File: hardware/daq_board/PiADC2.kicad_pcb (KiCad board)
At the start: 2 copper layers, 65 x 56 mm, 67 parts, among them J1 Pi GPIO, J2 ADCIN1, J3 ADCIN2, J4 ISO_IN, J6 I2C_OUT, SW1 SW_Push, SW2 SW_Push, U1 ADS1115IDGS, U2 TCA9517, U3 ADS1115IDGS, U4 24LC16, U5 MCP79401-I_SN, U6 MCP23008T-E_SS, U7 HCPL2631M, U8 HCPL2631M, Y1 Crystal

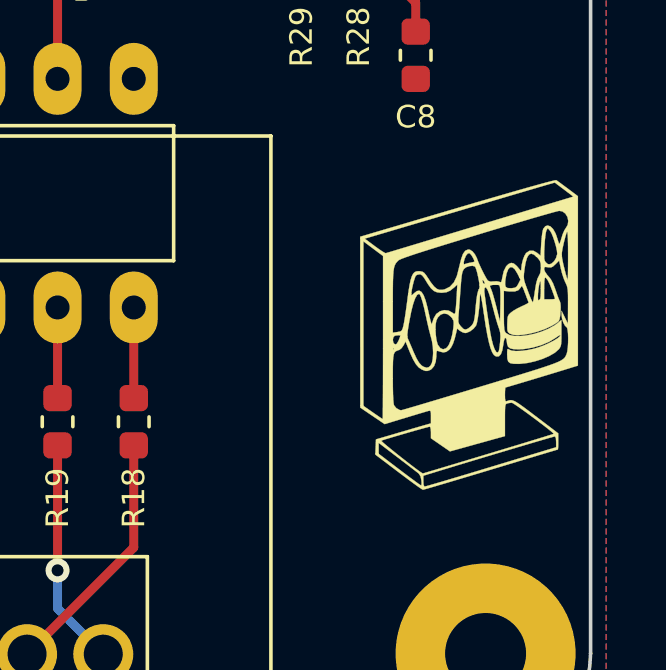
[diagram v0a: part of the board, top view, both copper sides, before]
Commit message: completed breakout board and updated daq board to version 2
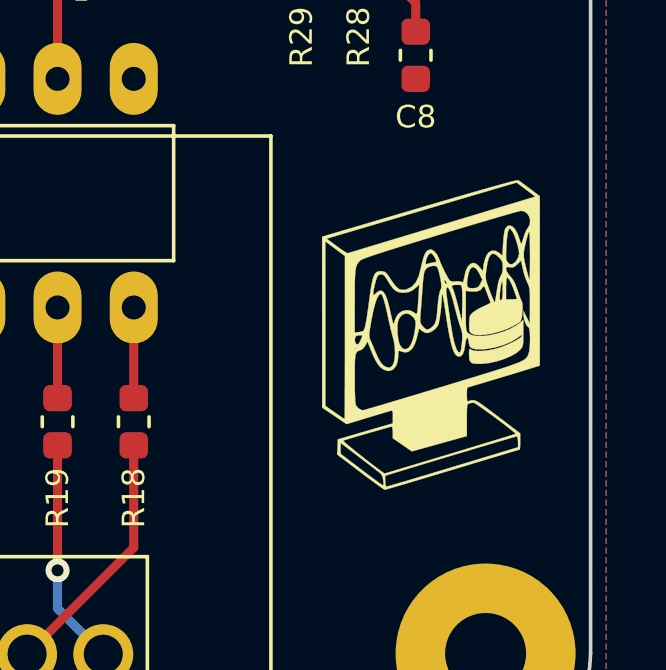
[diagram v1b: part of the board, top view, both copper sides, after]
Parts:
- moved LOGO1 1.27 mm to (166.9, 115.8)
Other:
- board text added: "FOR TESTING OR LABORATORY USE ONLY OPEN SOURCE HARDWARE RELEASED UNDER CERN OHL v1.2"
- board text added: "PiADC2 v2 CapConiX LLC capconix.com"
- board text removed: "FOR TESTING ONLY OPEN SOURCE HARDWARE RELEASED UNDER CERN OHL v1.2"
- board text removed: "PiADC2 v1 CapConiX LLC capconix.com"
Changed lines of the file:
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@@
   )
   (setup
-    (last_trace_width 0.3)
+    (last_trace_width 0.25)
     (user_trace_width 0.3)
     (trace_clearance 0.2)
@@
       (effects (font (size 0.75 0.75) (thickness 0.15)))
     )
-    (fp_text value ISO_IN (at 0 -4.445) (layer F.Fab)
+    (fp_text value ISO_IN (at 0 -4.445) (layer F.Fab) hide
       (effects (font (size 1 1) (thickness 0.15)))
     )
@@
   )
   (module CapConiX_Logos:CapConiX_Logo_10_7 (layer F.Cu)
-    (at 168.148 115.824)
+    (at 166.878 115.824)
     (fp_text reference LOGO1 (at 0 0) (layer F.SilkS) hide
       (effects (font (size 0.75 0.75) (thickness 0.3)))
@@
     )
   )
-  (gr_text "PiADC2 v1\nCapConiX LLC\ncapconix.com" (at 167.894 116.332 270) (layer B.SilkS)
+  (gr_text "PiADC2 v2\nCapConiX LLC\ncapconix.com" (at 166.878 116.332 270) (layer B.SilkS)
     (effects (font (size 1 1) (thickness 0.25)) (justify mirror))
   )
-  (gr_text "FOR TESTING ONLY\nOPEN SOURCE HARDWARE\nRELEASED UNDER CERN OHL v1.2" (at 148.59 101.6) (layer B.SilkS)
+  (gr_text "FOR TESTING OR LABORATORY USE ONLY\nOPEN SOURCE HARDWARE\nRELEASED UNDER CERN OHL v1.2" (at 148.59 101.6) (layer B.SilkS)
     (effects (font (size 1 1) (thickness 0.25)) (justify mirror))
   )
@@
   (segment (start 121.92 97.282) (end 121.928 97.29) (width 0.3) (layer F.Cu) (net 31))
   (segment (start 121.92 96.266) (end 121.92 97.282) (width 0.3) (layer F.Cu) (net 31))
+  (segment (start 119.6595 98.806) (end 120.65 98.806) (width 0.3) (layer F.Cu) (net 32))
+  (segment (start 120.65 98.806) (end 120.904 99.06) (width 0.3) (layer F.Cu) (net 32))
+  (segment (start 125.492 98.998) (end 125.492 98.298) (width 0.3) (layer F.Cu) (net 32))
+  (segment (start 125.43 99.06) (end 125.492 98.998) (width 0.3) (layer F.Cu) (net 32))
+  (segment (start 120.904 99.06) (end 125.43 99.06) (width 0.3) (layer F.Cu) (net 32))
+  (segment (start 121.003 97.926) (end 121.428 97.926) (width 0.3) (layer F.Cu) (net 32))
+  (segment (start 120.65 98.279) (end 121.003 97.926) (width 0.3) (layer F.Cu) (net 32))
+  (segment (start 120.65 98.806) (end 120.65 98.279) (width 0.3) (layer F.Cu) (net 32))
   (segment (start 119.6595 101.346) (end 120.65 101.346) (width 0.3) (layer F.Cu) (net 33))
   (segment (start 120.65 101.346) (end 120.904 101.092) (width 0.3) (layer F.Cu) (net 33))
@@
   (segment (start 120.65 101.873) (end 121.003 102.226) (width 0.3) (layer F.Cu) (net 33))
   (segment (start 120.65 101.346) (end 120.65 101.873) (width 0.3) (layer F.Cu) (net 33))
+  (segment (start 119.6595 103.886) (end 121.92 103.886) (width 0.3) (layer F.Cu) (net 34))
+  (segment (start 123.444 105.41) (end 125.492 105.41) (width 0.3) (layer F.Cu) (net 34))
+  (segment (start 121.92 103.886) (end 123.444 105.41) (width 0.3) (layer F.Cu) (net 34))
+  (segment (start 121.928 103.878) (end 121.92 103.886) (width 0.3) (layer F.Cu) (net 34))
+  (segment (start 121.928 102.226) (end 121.928 103.878) (width 0.3) (layer F.Cu) (net 34))
   (segment (start 121.92 115.824) (end 121.928 115.832) (width 0.3) (layer F.Cu) (net 35))
   (segment (start 121.928 115.832) (end 121.928 116.468) (width 0.3) (layer F.Cu) (net 35))
@@
   (segment (start 121.92 114.808) (end 123.444 113.284) (width 0.3) (layer F.Cu) (net 35))
   (segment (start 121.92 114.808) (end 121.92 115.824) (width 0.3) (layer F.Cu) (net 35))
-  (segment (start 125.43 119.634) (end 125.492 119.696) (width 0.3) (layer F.Cu) (net 37))
-  (segment (start 125.492 119.696) (end 125.492 120.396) (width 0.3) (layer F.Cu) (net 37))
-  (segment (start 121.003 120.768) (end 121.428 120.768) (width 0.3) (layer F.Cu) (net 37))
-  (segment (start 120.904 119.634) (end 125.43 119.634) (width 0.3) (layer F.Cu) (net 37))
-  (segment (start 120.65 119.888) (end 120.65 120.415) (width 0.3) (layer F.Cu) (net 37))
-  (segment (start 120.65 120.415) (end 121.003 120.768) (width 0.3) (layer F.Cu) (net 37))
-  (segment (start 119.6595 119.888) (end 120.65 119.888) (width 0.3) (layer F.Cu) (net 37))
-  (segment (start 120.65 119.888) (end 120.904 119.634) (width 0.3) (layer F.Cu) (net 37))
-  (segment (start 119.6595 98.806) (end 120.65 98.806) (width 0.3) (layer F.Cu) (net 32))
-  (segment (start 120.65 98.806) (end 120.904 99.06) (width 0.3) (layer F.Cu) (net 32))
-  (segment (start 125.492 98.998) (end 125.492 98.298) (width 0.3) (layer F.Cu) (net 32))
-  (segment (start 125.43 99.06) (end 125.492 98.998) (width 0.3) (layer F.Cu) (net 32))
-  (segment (start 120.904 99.06) (end 125.43 99.06) (width 0.3) (layer F.Cu) (net 32))
-  (segment (start 121.003 97.926) (end 121.428 97.926) (width 0.3) (layer F.Cu) (net 32))
-  (segment (start 120.65 98.279) (end 121.003 97.926) (width 0.3) (layer F.Cu) (net 32))
-  (segment (start 120.65 98.806) (end 120.65 98.279) (width 0.3) (layer F.Cu) (net 32))
-  (segment (start 119.6595 103.886) (end 121.92 103.886) (width 0.3) (layer F.Cu) (net 34))
-  (segment (start 123.444 105.41) (end 125.492 105.41) (width 0.3) (layer F.Cu) (net 34))
-  (segment (start 121.92 103.886) (end 123.444 105.41) (width 0.3) (layer F.Cu) (net 34))
-  (segment (start 121.928 103.878) (end 121.92 103.886) (width 0.3) (layer F.Cu) (net 34))
-  (segment (start 121.928 102.226) (end 121.928 103.878) (width 0.3) (layer F.Cu) (net 34))
   (segment (start 119.6595 117.348) (end 120.65 117.348) (width 0.3) (layer F.Cu) (net 36))
   (segment (start 120.65 116.821) (end 121.003 116.468) (width 0.3) (layer F.Cu) (net 36))
@@
   (segment (start 120.65 117.348) (end 120.65 116.821) (width 0.3) (layer F.Cu) (net 36))
   (segment (start 125.492 117.54) (end 125.492 116.84) (width 0.3) (layer F.Cu) (net 36))
+  (segment (start 125.43 119.634) (end 125.492 119.696) (width 0.3) (layer F.Cu) (net 37))
+  (segment (start 125.492 119.696) (end 125.492 120.396) (width 0.3) (layer F.Cu) (net 37))
+  (segment (start 121.003 120.768) (end 121.428 120.768) (width 0.3) (layer F.Cu) (net 37))
+  (segment (start 120.904 119.634) (end 125.43 119.634) (width 0.3) (layer F.Cu) (net 37))
+  (segment (start 120.65 119.888) (end 120.65 120.415) (width 0.3) (layer F.Cu) (net 37))
+  (segment (start 120.65 120.415) (end 121.003 120.768) (width 0.3) (layer F.Cu) (net 37))
+  (segment (start 119.6595 119.888) (end 120.65 119.888) (width 0.3) (layer F.Cu) (net 37))
+  (segment (start 120.65 119.888) (end 120.904 119.634) (width 0.3) (layer F.Cu) (net 37))
   (segment (start 123.444 123.952) (end 125.492 123.952) (width 0.3) (layer F.Cu) (net 38))
   (segment (start 119.6595 122.428) (end 121.92 122.428) (width 0.3) (layer F.Cu) (net 38))

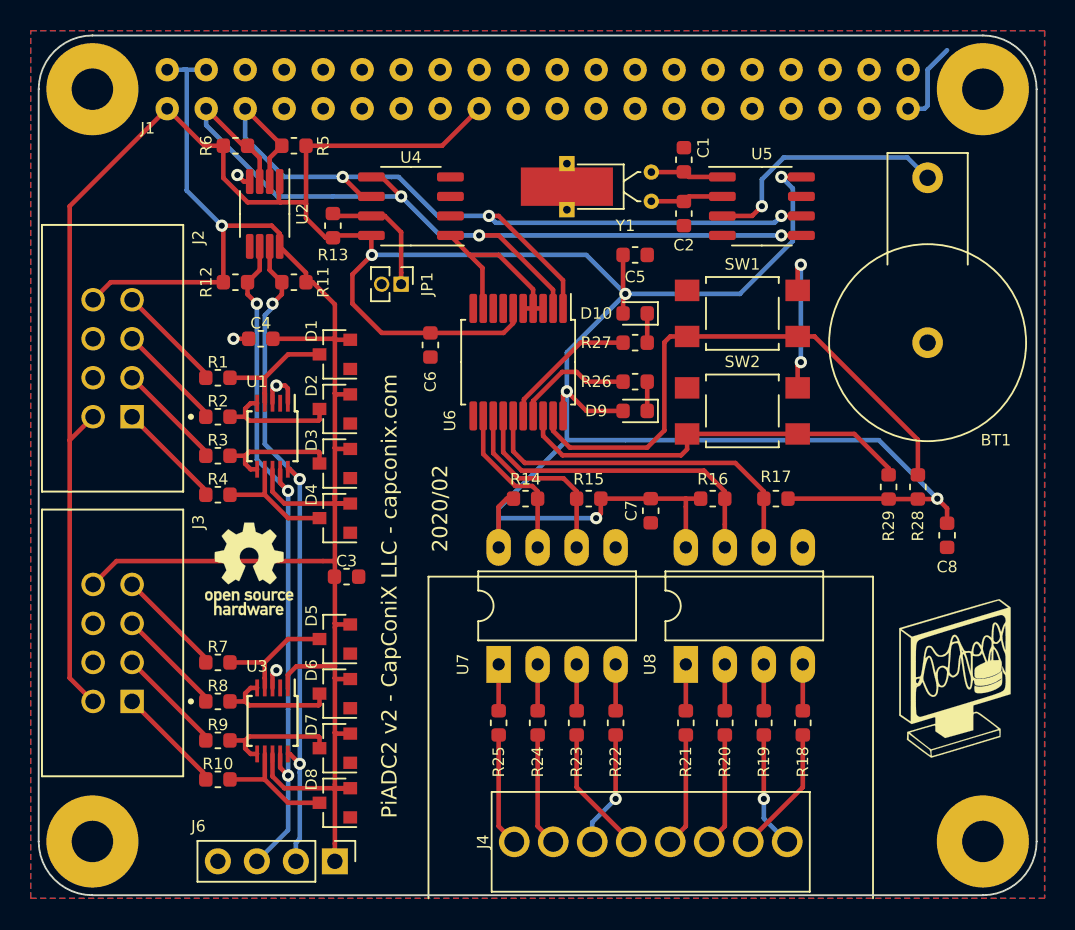
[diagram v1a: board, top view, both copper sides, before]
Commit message: Updated V2 to include an environmental sensor
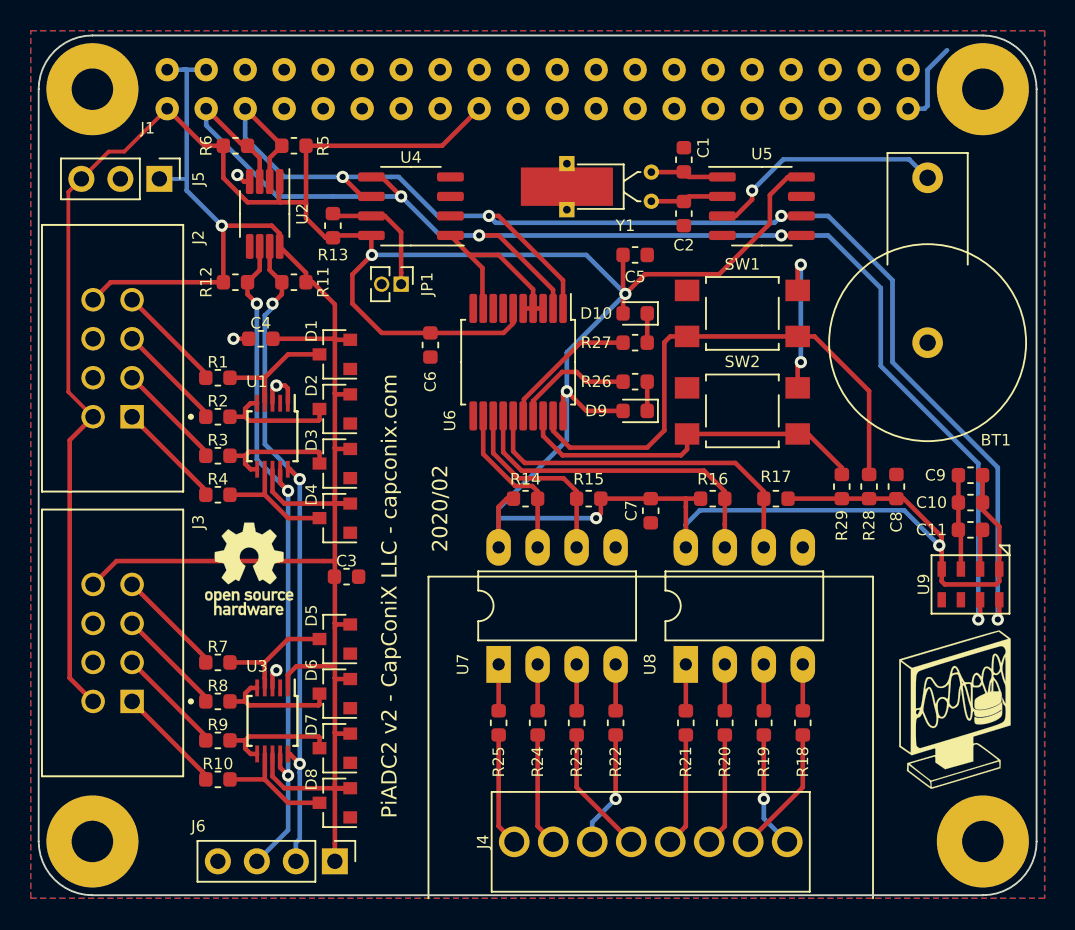
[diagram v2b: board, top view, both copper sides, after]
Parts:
- added C10: 0.1uF, Capacitor_SMD:C_0603_1608Metric, F.Cu at (167.9, 104.4)
- added C11: 0.1uF, Capacitor_SMD:C_0603_1608Metric, F.Cu at (167.9, 106.2)
- added C9: 10uF, Capacitor_SMD:C_0603_1608Metric, F.Cu at (167.9, 102.6)
- added J5: AUX_POWER, Connector_PinHeader_2.54mm:PinHeader_1x03_P2.54mm_Vertical, F.Cu at (115.1, 83.3)
- added U9: MPL3115A2, MPL3115A2:MPL3115A2, F.Cu at (167.9, 109.7)
- moved C8 4.58 mm to (163.1, 103.4), turned to 270 degrees
- moved R28 3.18 mm to (161.3, 103.4)
- moved R29 3.05 mm to (159.5, 103.4)
- moved LOGO1 2.03 mm to (166.9, 117.9)
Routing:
- net I2C_SCL_3V3: track 57.5 -> 92.7 mm, vias 3 -> 4
- net I2C_SDA_3V3: track 59.1 -> 92.6 mm, vias 3 -> 4
- net GND: track 34.9 -> 41.1 mm
- net +3V3: track 221.6 -> 226.6 mm, vias 6 -> 5
- net Net-(R29-Pad2): track 26.9 -> 23.8 mm
- net Net-(C11-Pad2): track 0.00 -> 2.62 mm
- net +5V: track 119.7 -> 121.5 mm
- net Net-(R28-Pad2): track 36.6 -> 35.3 mm
- net Net-(BT1-Pad1): track 16.5 -> 15.7 mm
